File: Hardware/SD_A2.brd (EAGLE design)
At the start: 100.2 x 77.7 mm, 32 parts, among them IC1 74LS245N, IC2 LM317, IC3 2716 / 2732, IC4 XC9572XL

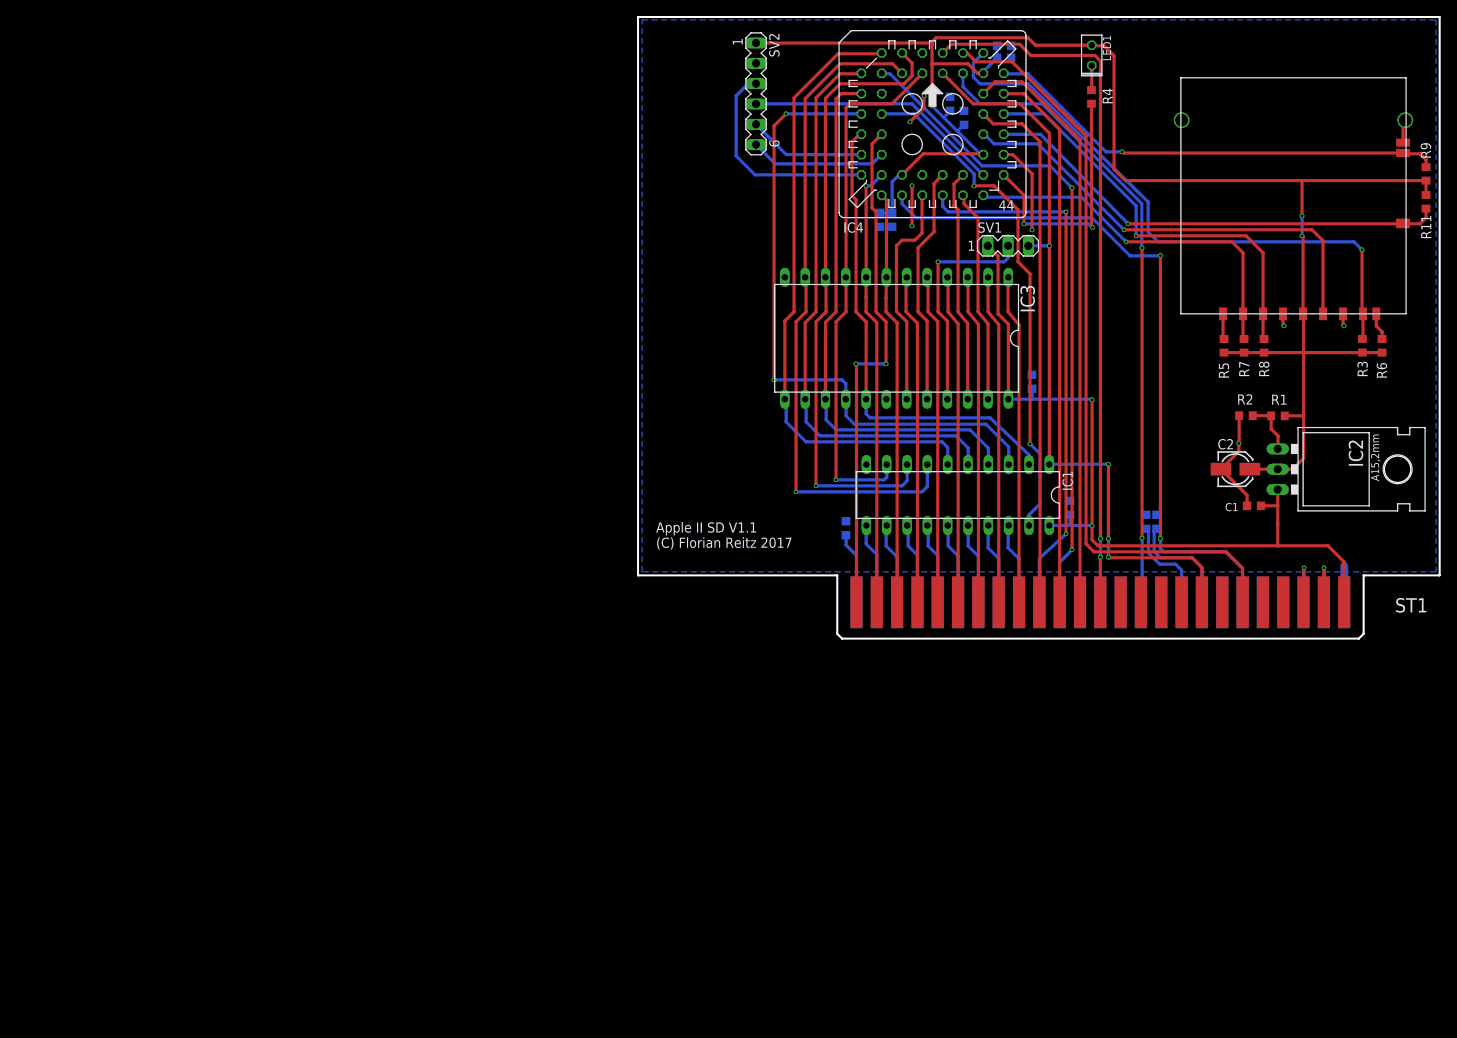
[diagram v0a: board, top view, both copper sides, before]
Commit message: Replace CPLD with MC6852 and add Level Shifting microSD Breakout.
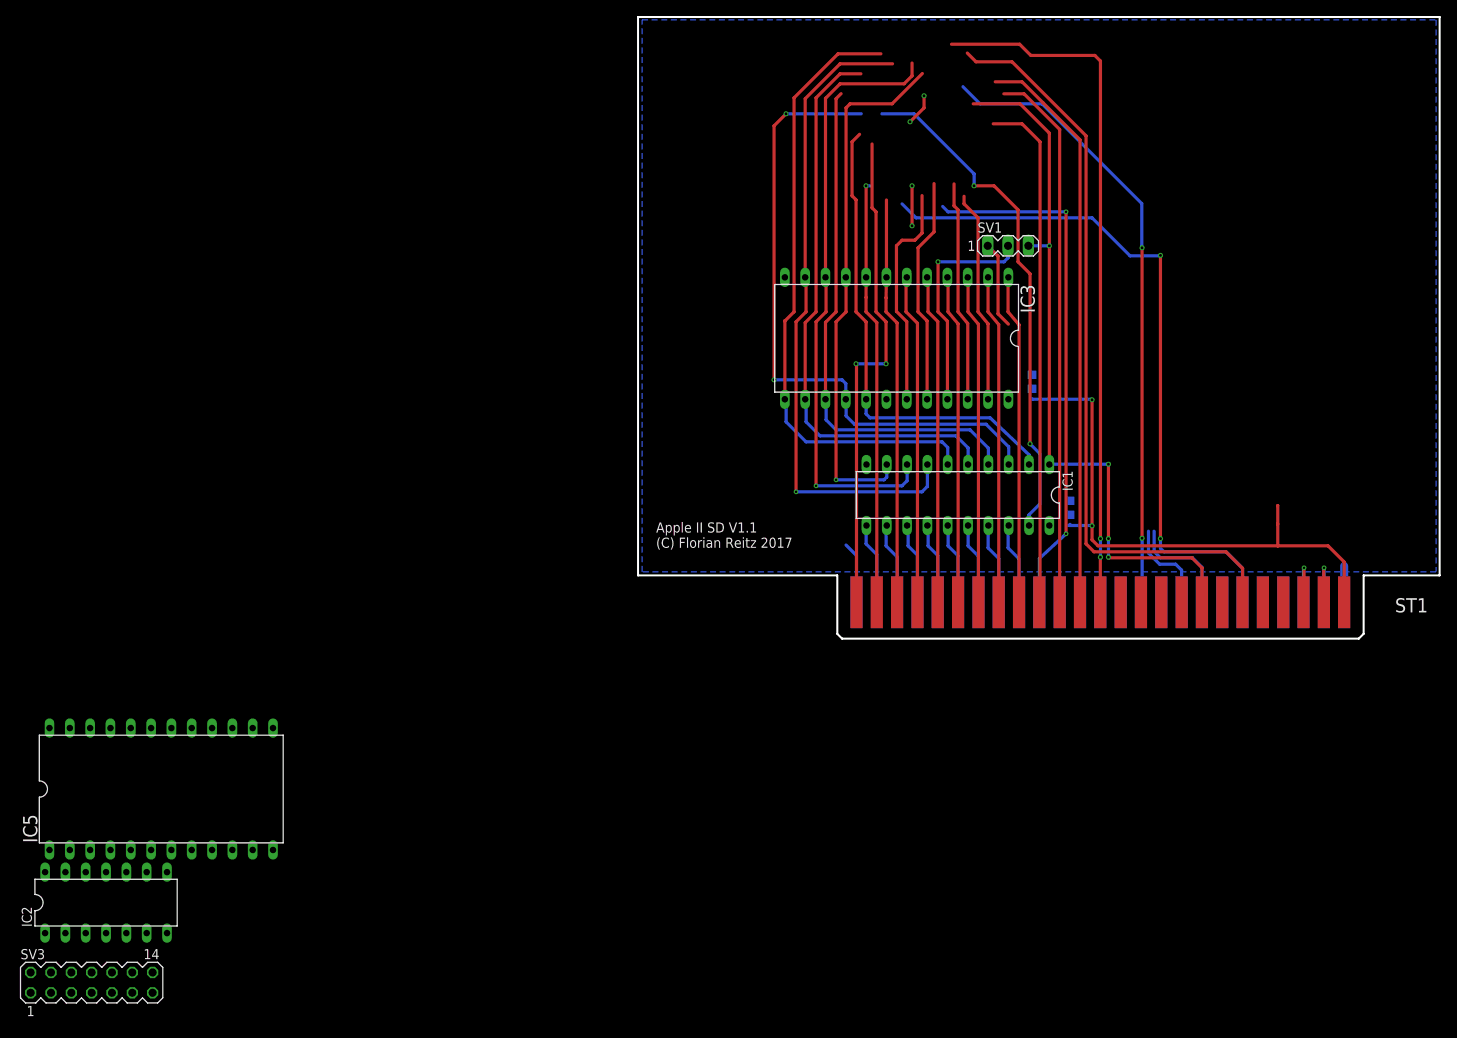
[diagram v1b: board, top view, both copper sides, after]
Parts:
- removed C1, C11, C12, C13, C5, C6, C7: 100n, rcl:C0603K
- removed C10, C8, C9: 10n, rcl:C0603K
- removed C2: 1u, rcl:153CLV-0405
- removed IC4: XC9572XL, xilinx-xc9:S44
- removed LED1: (no value), led:LED2X5
- removed R1: 200, rcl:R0603
- removed R11, R3, R5, R6, R7, R9: 100k, rcl:R0603
- removed R2: 330, rcl:R0603
- removed R4: 470, rcl:R0603
- removed R8: 68k, rcl:R0603
- removed SV2: (no value), con-lstb:MA06-1
- removed U$2: 104H-TDA0-R, con-sd-attend2:104H-TDA0-R
- added IC5: (no value), micro-motorola:DIL24
- added SV3: (no value), con-lstb:MA07-2
- IC2: value LM317 -> 74LS04N; device v-reg:317TL -> 74xx-us:DIL14
- moved IC2 159.7 mm to (-66.5, -33.1), turned to 0 degrees
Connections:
- removed net !G: IC1.19, IC4.12
- removed net !LED: IC4.29, R4.2
- removed net +3V3: C10.1, C2.+, C5.1, C6.1, C7.1, C8.1, C9.1, IC2.2, IC4.21, IC4.32, IC4.41, LED1.A, R1.2, R11.1, R3.2, R5.1, R6.1, R7.2, R8.2, R9.1, SV2.1, U$2.P4
- removed net CARD: IC4.33, R11.2, U$2.CD
- removed net N$29: LED1.K, R4.1
- removed net N$3: R6.2, U$2.P8
- removed net PHI_0: IC4.8, ST1.40
- removed net TCK: IC4.17, SV2.3
- removed net TDI: IC4.15, SV2.5
- removed net TDO: IC4.30, SV2.4
- removed net TMS: IC4.16, SV2.6
- removed net WP: IC4.39, R9.2, U$2.WP
- new net !CD: IC5.24, SV3.11
- new net PHI_1: IC2.1, ST1.38
- new net PHI_2*: IC2.6, IC5.14
- new net VCC: IC2.14, IC5.12
- new net VSS: IC5.1
- net !CS: now also IC5.5, SV3.3; no longer IC4.28, R7.1, U$2.P1
- net !DEV_SEL: now also IC1.19, IC5.10; no longer IC4.24
- net !IO_SEL: no longer IC4.14
- net !IO_STR: no longer IC4.42
- net !OE: no longer IC4.25
- net !RESET: now also IC5.9; no longer IC4.20
- net +12V: no longer C11.1
- net +5V: now also SV3.1; no longer C1.1, IC2.3
- net -12V: no longer C12.1
- net -5V: no longer C13.1
- net 7M: no longer IC4.43
- net ADD0: now also IC5.11; no longer IC4.19
- net ADD1: no longer IC4.18
- net ADD10: no longer IC4.38
- net ADD11: no longer IC4.44
- net ADD8: no longer IC4.36
- net ADD9: no longer IC4.37
- net B10: no longer IC4.22
- net B8: no longer IC4.26
- net B9: no longer IC4.27
- net CLK: now also IC5.3, IC5.4, SV3.7; no longer IC4.34, U$2.P5
- net DATA0: now also IC5.22; no longer IC4.3
- net DATA1: now also IC5.21; no longer IC4.4
- net DATA2: now also IC5.20; no longer IC4.5
- net DATA3: now also IC5.19; no longer IC4.6
- net DATA4: now also IC5.18; no longer IC4.7
- net DATA5: now also IC5.17; no longer IC4.9
- net DATA6: now also IC5.16; no longer IC4.11
- net DATA7: now also IC5.15; no longer IC4.13
- net GND: now also IC2.7, IC5.23, SV3.13; no longer C1.2, C10.2, C11.2, C12.2, C13.2, C2.-, C5.2, C6.2, C7.2, C8.2, C9.2, IC4.10, IC4.23, IC4.31, R2.1, SV2.2, U$2.GND0, U$2.GND1, U$2.P3, U$2.P6, U$2.SC
- net MISO: now also IC5.2, SV3.9; no longer IC4.40, R3.1, U$2.P7
- net MOSI: now also IC5.6, SV3.5; no longer IC4.35, R8.1, U$2.P2
- net N$1: now also IC2.2, IC2.3; no longer IC2.1, R1.1, R2.2
- net N$2: now also IC2.4, IC2.5; no longer R5.2, U$2.P9
- net R/!W: now also IC5.13; no longer IC4.1
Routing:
- net +3V3: track 214.5 -> 0.00 mm, vias 3 -> 0
- net PHI_0: track 82.2 -> 0.00 mm, vias 2 -> 0
- net MISO: track 74.4 -> 0.00 mm, vias 1 -> 0
- net !G: track 64.1 -> 0.00 mm, vias 2 -> 0
- net !DEV_SEL: track 67.4 -> 130.0 mm, vias 2 -> 4
- net CARD: track 59.0 -> 0.00 mm, vias 1 -> 0
- net WP: track 58.2 -> 0.00 mm, vias 1 -> 0
- net CLK: track 57.1 -> 0.00 mm, vias 1 -> 0
- net MOSI: track 52.6 -> 0.00 mm, vias 1 -> 0
- net !CS: track 46.3 -> 0.00 mm, vias 1 -> 0
- net TDO: track 32.1 -> 0.00 mm
- net !LED: track 31.4 -> 0.00 mm, vias 2 -> 0
- net GND: track 44.8 -> 13.5 mm, vias 8 -> 4
- net TCK: track 27.3 -> 0.00 mm
- net +5V: track 103.2 -> 81.8 mm
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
